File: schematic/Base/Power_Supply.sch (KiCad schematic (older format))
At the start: 78 parts, among them J201 Conn_01x03, Q201 TIP42C, Q202 TIP42C, Q203 TIP41C, Q204 BCP56, Q205 BCP56, Q206 BCP53, U201 TL431PK, U202 TL431PK, U203 TL431PK

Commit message: Base schematic complete
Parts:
- added C228: 2.2uF, Capacitor_SMD:C_0603_1608Metric, symbol Device:C
- added C229, C233: 100nF, Capacitor_SMD:C_0603_1608Metric, symbol Device:C
- added C230, C235: 100uF/10V, Capacitor_SMD:C_Elec_6.3x5.4, symbol Device:CP
- added C231, C234: 10uF, Capacitor_SMD:C_0603_1608Metric, symbol Device:C
- added C232: 10nF, Capacitor_SMD:C_0603_1608Metric, symbol Device:C
- added JP201: Jumper_NO_Small, Connector_PinSocket_2.54mm:PinSocket_1x02_P2.54mm_Vertical, symbol Device:Jumper_NO_Small
- added L201: 18uH, Inductor_THT:L_Radial_D7.5mm_P3.50mm_Fastron_07P, symbol Device:L_Core_Ferrite
- added U204: AM2D-0503SZ, Zmei_Footprints:Converter_DCDC_AM2D, symbol Zmei_elements:AM2D-0503SZ
- added U205: TPS73633DCQ, Package_TO_SOT_SMD:SOT-223-6_TabPin3, symbol Zmei_elements:TPS73601DCQ
- R206, R207, R218, R219, R221, R222: footprint Resistor_SMD:R_1206_3216Metric -> Resistor_SMD:R_0603_1608Metric
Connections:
- net +5V: now also JP201.2
- net GND: now also C206.2, C212.2, C217.2, C222.2, C225.2, D202.2 (A), D208.2 (A), R213.2, R220.1, U203.2 (A), C228.1, C229.1, C230.2, C231.1, C232.1, C234.1, C235.2, U204.2 (-Vin), U205.3 (GND)
- new net: C228.2, C230.1, C231.2, JP201.1, L201.2, U205.1 (IN), U205.5 (EN)
- new net: C229.2, L201.1, U204.1 (+Vin)
- new net: C232.2, U205.4 (FB)
- new net +3V3_IO: C234.2, C235.1, U205.2 (OUT)
- new net +3V3_ISOL: C233.2, U204.6 (+Vout)
- new net GNDD: C233.1, U204.4 (-Vout)
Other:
- moved on the sheet: C201, C202, C203, C204, C205, C206, C207, C208, C209, C210, C211, C212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

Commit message: Check-in of misc. sch changes to Base
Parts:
- removed C202, C203, C204: C, Capacitor_THT:C_Rect_L11.0mm_W5.1mm_P10.00mm_MKT, symbol Device:C
- removed D201, D202, D207, D208: SR580, Diode_THT:D_DO-27_P15.24mm_Horizontal, symbol Device:D
- removed D203, D204, D205, D206, D209, D210, D211, D212: 1N5400, Diode_THT:D_DO-27_P15.24mm_Horizontal, symbol Device:D
- removed R202, R203, R204: R, Resistor_THT:R_Axial_DIN0207_L6.3mm_D2.5mm_P10.16mm_Horizontal, symbol Device:R
- removed TR201: TRAF_BULTRAF10VA_SINGLE, Zmei_Footprints:TRAF_BULTRAF10VA, symbol Zmei_elements:TRAF_BULTRAF10VA_SINGLE
- removed TR202: ANG_6VA, Zmei_Footprints:TRAF_ANG6VA, symbol Zmei_elements:ANG_6VA
- added D201, D202, D216: KBU8M, Diode_THT:Diode_Bridge_Vishay_KBU, symbol Diode_Bridge:KBU8M
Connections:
- net GND: now also D201.4 (-), D202.1 (+), D216.4 (-)
- net at C211.2, C212.1, TR204.6: now also D201.2 (~~)
- net at C205.2, C206.1, TR204.5: now also D201.3 (~~)
- net at C205.1, C211.1, C217.1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: now also D201.1 (+)
- net at C209.2, C210.1, TR203.3: now also D202.3 (~~)
- net at C215.2, C216.1, TR203.4: now also D202.2 (~~)
- net at C207.2, C208.1: now also TR203.6, D216.3 (~~); no longer TR203.5
- net at C213.2, C214.1: now also TR203.5, D216.2 (~~); no longer TR203.6
- net at C207.1, C213.1, C218.1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: now also D216.1 (+)
- net at C210.2, C216.2, C219.2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: now also D202.4 (-)

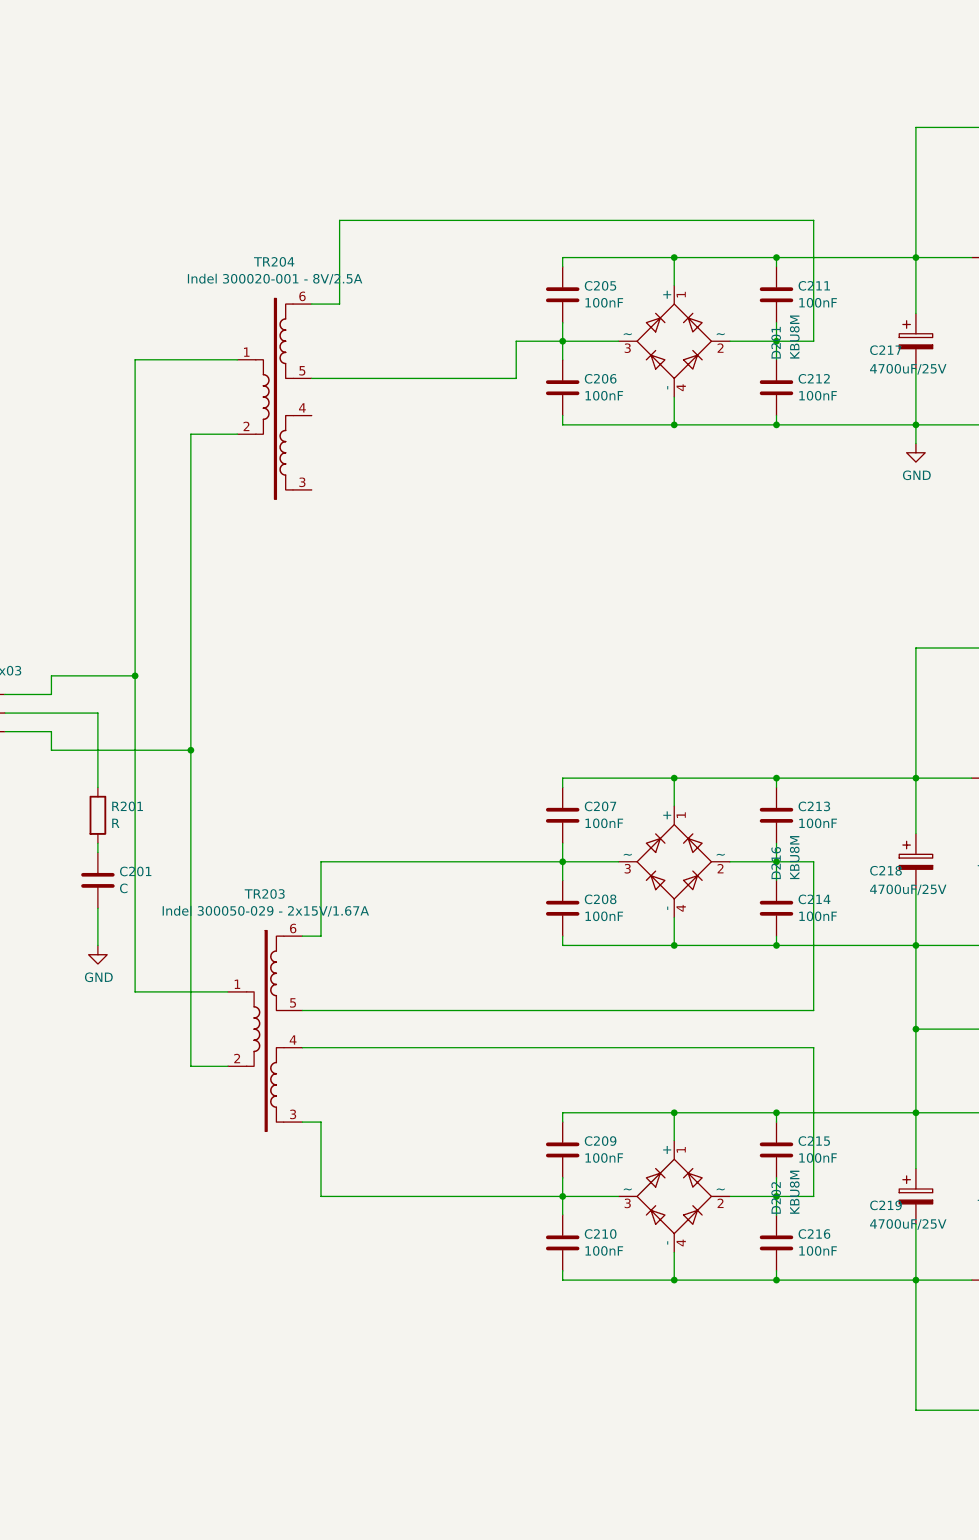
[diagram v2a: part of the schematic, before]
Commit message: Add Changes.txt, listing future changes to the schematic and boards Finish up Base board routing
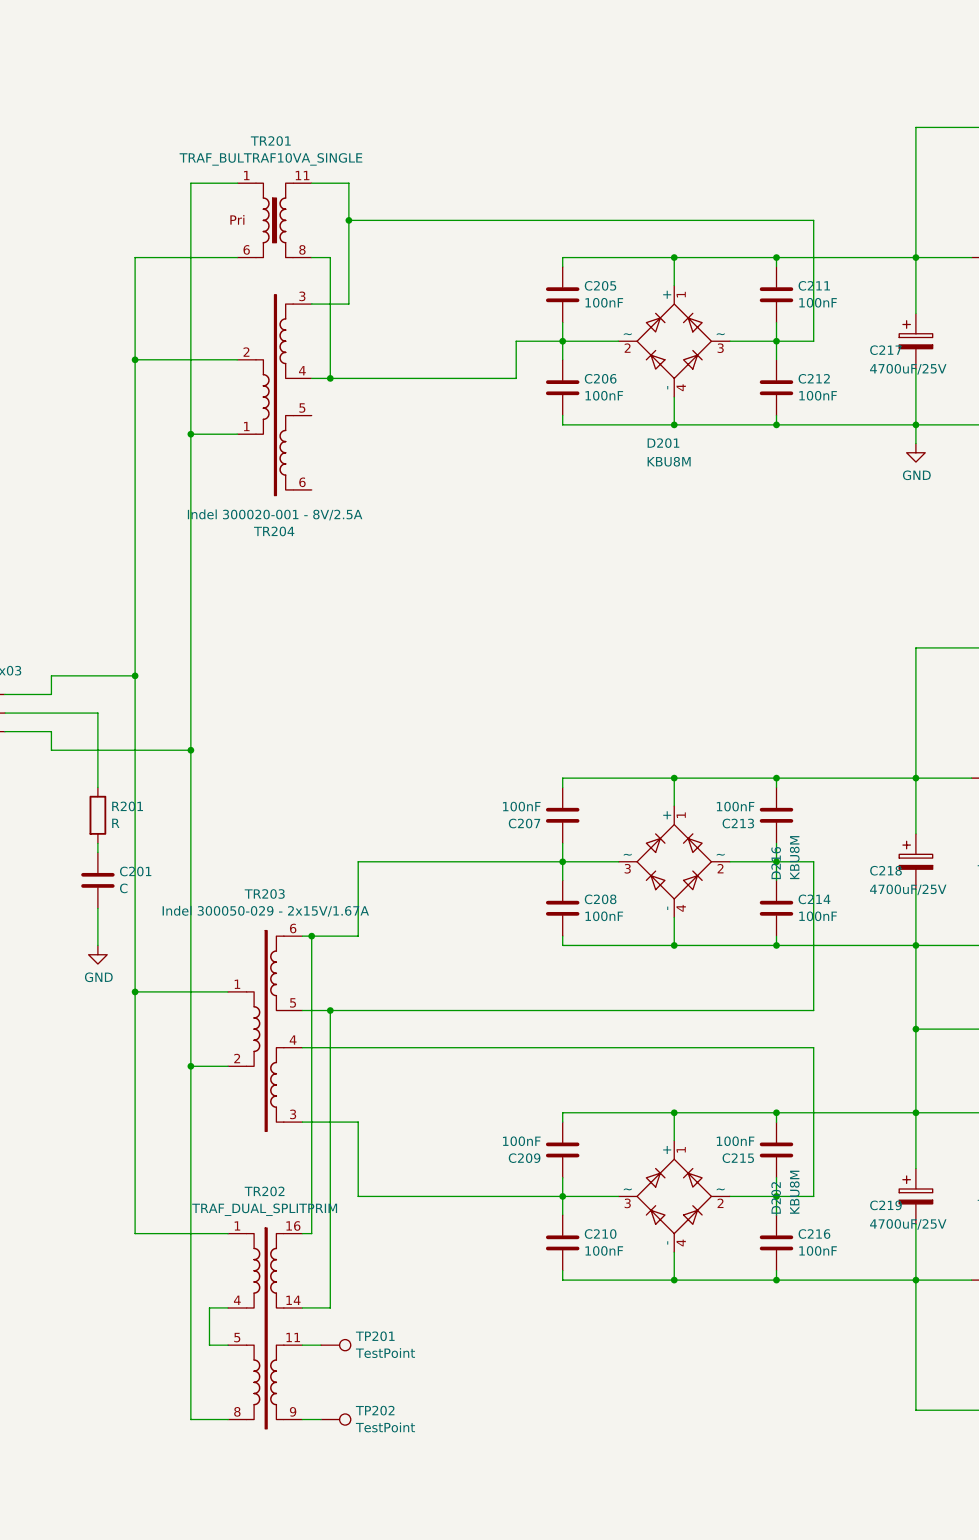
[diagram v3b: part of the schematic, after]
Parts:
- added TP201, TP202: TestPoint, TestPoint:TestPoint_THTPad_D2.0mm_Drill1.0mm, symbol Connector:TestPoint
- added TR201: TRAF_BULTRAF10VA_SINGLE, Zmei_Footprints:TRAF_BULTRAF10VA, symbol Zmei_elements:TRAF_BULTRAF10VA_SINGLE
- added TR202: TRAF_DUAL_SPLITPRIM, Zmei_Footprints:TRAF_ANG_DUAL_18_24VA, symbol Zmei_elements:TRAF_DUAL_SPLITPRIM
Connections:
- net GND: now also C209.2, C215.2; no longer C209.1, C215.1
- net at C218.1, D214.1 (K), D216.1 (+)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: now also C207.2, C213.2; no longer C207.1, C213.1
- net at C214.1, D216.2 (~~), TR203.5: now also C213.1, TR202.14; no longer C213.2
- net at C208.1, D216.3 (~~), TR203.6: now also C207.1, TR202.16; no longer C207.2
- net at C216.1, D202.2 (~~), TR203.4: now also C215.1; no longer C215.2
- net at C210.1, D202.3 (~~), TR203.3: now also C209.1; no longer C209.2
- net at C211.2, C212.1: now also D201.3 (~~), TR204.3, TR201.11; no longer D201.2 (~~), TR204.6
- net at C205.2, C206.1: now also D201.2 (~~), TR204.4, TR201.8; no longer D201.3 (~~), TR204.5
- net at J201.1 (Pin_1), TR203.1: now also TR204.2, TR201.6, TR202.1; no longer TR204.1
- net at J201.3 (Pin_3), TR203.2: now also TR204.1, TR201.1, TR202.8; no longer TR204.2
- new net: TP201.1, TR202.11
- new net: TR202.4, TR202.5
- new net: TP202.1, TR202.9
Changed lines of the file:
@@
 F 3 "" H 3600 5050 50  0001 C CNN
 	1    3050 5050
-	1    0    0    -1
+	1    0    0    1
 $EndComp
 $Comp
@@
 	2100 8000 2100 7800
 Wire Wire Line
-	3400 4550 3250 4550
+	3450 4550 3250 4550
 $Comp
 L Device:C C205
@@
 F 3 "~" H 4600 7300 50  0001 C CNN
 	1    4600 7300
-	1    0    0    -1
+	-1   0    0    1
 $EndComp
 Wire Wire Line
@@
 F 3 "~" H 5750 7300 50  0001 C CNN
 	1    5750 7300
-	1    0    0    -1
+	-1   0    0    1
 $EndComp
 $Comp
@@
 F 3 "~" H 4600 9100 50  0001 C CNN
 	1    4600 9100
-	1    0    0    -1
+	-1   0    0    1
 $EndComp
 Wire Wire Line
@@
 F 3 "~" H 5750 9100 50  0001 C CNN
 	1    5750 9100
-	1    0    0    -1
+	-1   0    0    1
 $EndComp
 $Comp
@@
 U 1 1 5E5C061F
 P 5200 4750
-F 0 "D201" H 5100 4200 50  0000 L CNN
-F 1 "KBU8M" H 5100 4100 50  0000 L CNN
+F 0 "D201" V 4650 4600 50  0000 L CNN
+F 1 "KBU8M" V 4550 4600 50  0000 L CNN
 F 2 "Diode_THT:Diode_Bridge_Vishay_KBU" H 5350 4875 50  0001 L CNN
 F 3 "http://www.vishay.com/docs/88656/kbu8.pdf" H 5200 4750 50  0001 C CNN
 	1    5200 4750
-	0    -1   -1   0
+	0    1    -1   0
 $EndComp
 Wire Wire Line
@@
 	5950 8350 5950 7550
 Wire Wire Line
-	3200 8350 5950 8350
-Wire Wire Line
-	3200 7950 3300 7950
-Wire Wire Line
-	3300 7950 3300 7550
-Wire Wire Line
-	3300 7550 4600 7550
+	3200 8350 3350 8350
+Wire Wire Line
+	3200 7950 3250 7950
+Wire Wire Line
+	3500 7950 3500 7550
+Wire Wire Line
+	3500 7550 4600 7550
 Wire Wire Line
 	5950 8550 5950 9350
@@
 	3200 8550 5950 8550
 Wire Wire Line
-	3200 8950 3300 8950
-Wire Wire Line
-	3300 8950 3300 9350
-Wire Wire Line
-	3300 9350 4600 9350
-Wire Wire Line
-	3400 4100 5950 4100
-Wire Wire Line
-	3400 4100 3400 4550
-Wire Wire Line
-	3250 4950 4350 4950
+	3200 8950 3500 8950
+Wire Wire Line
+	3500 8950 3500 9350
+Wire Wire Line
+	3500 9350 4600 9350
+Wire Wire Line
+	3450 4100 5950 4100
+Wire Wire Line
+	3450 4100 3450 4550
+Wire Wire Line
+	3250 4950 3350 4950
+$Comp
+L Zmei_elements:TRAF_BULTRAF10VA_SINGLE TR201
+U 1 1 5E4F305C
+P 3050 4100
+F 0 "TR201" H 3033 4525 50  0000 C CNN
+F 1 "TRAF_BULTRAF10VA_SINGLE" H 3033 4434 50  0000 C CNN
+F 2 "Zmei_Footprints:TRAF_BULTRAF10VA" H 3050 4100 50  0001 C CNN
+F 3 "" H 3050 4100 50  0001 C CNN
+	1    3050 4100
+	1    0    0    -1
+$EndComp
+Wire Wire Line
+	2300 4850 2300 4300
+Connection ~ 2300 4850
+Connection ~ 2600 5250
+Wire Wire Line
+	3250 4300 3350 4300
+Wire Wire Line
+	3350 4300 3350 4950
+Connection ~ 3350 4950
+Wire Wire Line
+	3350 4950 4350 4950
+Wire Wire Line
+	3250 3900 3450 3900
+Wire Wire Line
+	3450 3900 3450 4100
+Connection ~ 3450 4100
+Wire Wire Line
+	2850 3900 2600 3900
+Wire Wire Line
+	2600 3900 2600 5250
+Wire Wire Line
+	2850 4300 2300 4300
+$Comp
+L Zmei_elements:TRAF_DUAL_SPLITPRIM TR202
+U 1 1 5E5CB980
+P 3000 10050
+F 0 "TR202" H 3000 10775 50  0000 C CNN
+F 1 "TRAF_DUAL_SPLITPRIM" H 3000 10684 50  0000 C CNN
+F 2 "Zmei_Footprints:TRAF_ANG_DUAL_18_24VA" H 3550 10350 50  0001 C CNN
+F 3 "" H 3550 10050 50  0001 C CNN
+	1    3000 10050
+	1    0    0    -1
+$EndComp
+Wire Wire Line
+	2800 10150 2700 10150
+Wire Wire Line
+	2700 10150 2700 9950
+Wire Wire Line
+	2700 9950 2800 9950
+Wire Wire Line
+	2600 8650 2600 10550
+Wire Wire Line
+	2600 10550 2800 10550
+Connection ~ 2600 8650
+Wire Wire Line
+	2800 9550 2300 9550
+Wire Wire Line
+	2300 9550 2300 8250
+Connection ~ 2300 8250
+Wire Wire Line
+	3200 9550 3250 9550
+Wire Wire Line
+	3250 9550 3250 7950
+Connection ~ 3250 7950
+Wire Wire Line
+	3250 7950 3500 7950
+Wire Wire Line
+	3350 8350 3350 9950
+Wire Wire Line
+	3350 9950 3200 9950
+Connection ~ 3350 8350
+Wire Wire Line
+	3350 8350 5950 8350
+$Comp
+L Connector:TestPoint TP201
+U 1 1 5E6728EE
+P 3300 10150
+F 0 "TP201" V 3254 10338 50  0000 L CNN
+F 1 "TestPoint" V 3345 10338 50  0000 L CNN
+F 2 "TestPoint:TestPoint_THTPad_D2.0mm_Drill1.0mm" H 3500 10150 50  0001 C CNN
+F 3 "~" H 3500 10150 50  0001 C CNN
+	1    3300 10150
+	0    1    1    0
+$EndComp
+$Comp
+L Connector:TestPoint TP202
+U 1 1 5E673797
+P 3300 10550
+F 0 "TP202" V 3254 10738 50  0000 L CNN
+F 1 "TestPoint" V 3345 10738 50  0000 L CNN
+F 2 "TestPoint:TestPoint_THTPad_D2.0mm_Drill1.0mm" H 3500 10550 50  0001 C CNN
+F 3 "~" H 3500 10550 50  0001 C CNN
+	1    3300 10550
+	0    1    1    0
+$EndComp
+Wire Wire Line
+	3300 10550 3200 10550
+Wire Wire Line
+	3200 10150 3300 10150
 $EndSCHEMATC
